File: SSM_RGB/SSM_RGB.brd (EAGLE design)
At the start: 80.1 x 68.8 mm, 12 parts

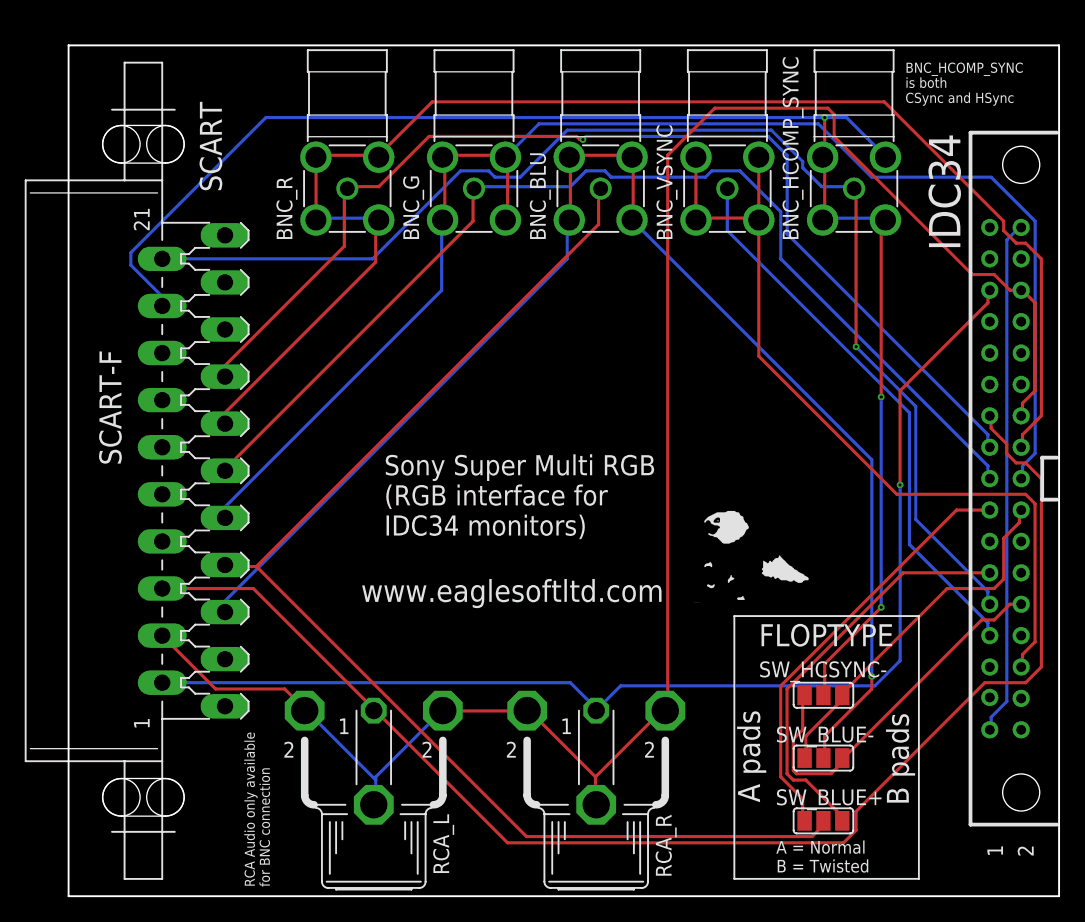
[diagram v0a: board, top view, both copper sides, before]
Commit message: Final PCB revisions
SSM & X:
*Renamed BNC_HComp_Sync to just BNC_HCSYNC
*Renamed "Normal" cable type to "Nonstd"
*Removed stray line segs in PCB Art

SSM:
*Added warning about using both AV sources

X:
*Renamed VReg and Bus Sw IC components to Ux series
*Renamed both switchs to Sx series
*Renamed "PWR" to "J1"

Documentation:
*1st draft. Needs final product photos/images, and list of component names+parts
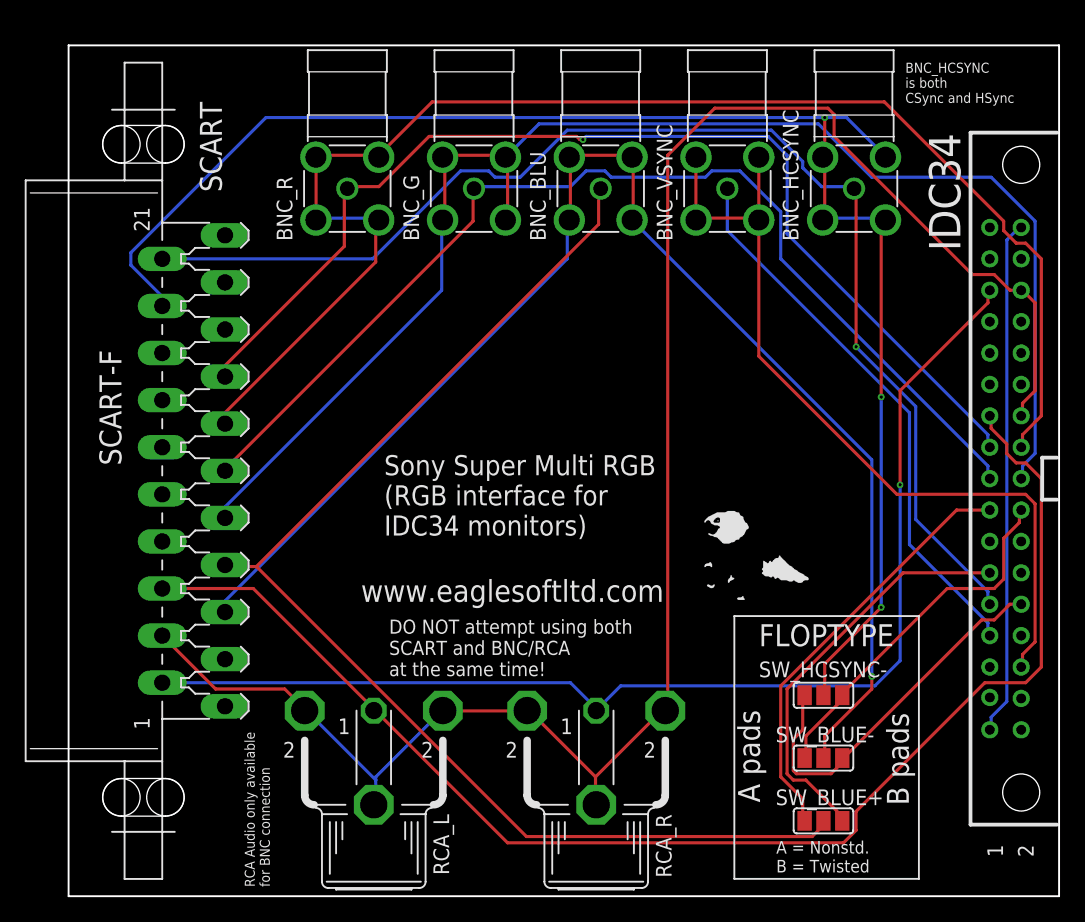
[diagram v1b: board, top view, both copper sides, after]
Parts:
- renumbered BNC_HCOMP_SYNC to BNC_HCSYNC
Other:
- board text added: "A = Nonstd. B = Twisted"
- board text added: "BNC_HCSYNC is both CSync and HSync"
- board text added: "DO NOT attempt using both SCART and BNC/RCA at the same time!"
- board text removed: "A = Normal B = Twisted"
- board text removed: "BNC_HCOMP_SYNC is both CSync and HSync"
- board text removed: "C:/Users/Anthony/Documents/eagle/SSM/Artwork/Large/p1m.bmp"
- board text removed: "C:/Users/Anthony/Documents/eagle/SSM/Artwork/Large/p2m.bmp"
- board text removed: "C:/Users/Anthony/Documents/eagle/SSM/Artwork/Large/p3m.bmp"
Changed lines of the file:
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@@
 (RGB interface for
 IDC34 monitors)</text>
-<text x="137.2997" y="36.72205" size="1.016" layer="21">A = Normal
+<text x="137.2997" y="36.72205" size="1.016" layer="21">A = Nonstd.
 B = Twisted</text>
-<text x="147.74545" y="98.97745" size="0.8128" layer="21">BNC_HCOMP_SYNC
+<text x="147.74545" y="98.97745" size="0.8128" layer="21">BNC_HCSYNC
 is both
 CSync and HSync</text>
@@
 <rectangle x1="135.912225" y1="71.034275" x2="136.998075" y2="71.040625" layer="17"/>
 <rectangle x1="135.912225" y1="71.040625" x2="136.998075" y2="71.046975" layer="17"/>
-<text x="130.63855" y="58.52795" size="0.0127" layer="17" font="vector">C:/Users/Anthony/Documents/eagle/SSM/Artwork/Large/p1m.bmp</text>
 <rectangle x1="134.750175" y1="58.874025" x2="134.877175" y2="58.880375" layer="29"/>
 <rectangle x1="134.750175" y1="58.880375" x2="134.877175" y2="58.886725" layer="29"/>
@@
 <rectangle x1="135.912225" y1="71.034275" x2="136.998075" y2="71.040625" layer="29"/>
 <rectangle x1="135.912225" y1="71.040625" x2="136.998075" y2="71.046975" layer="29"/>
-<text x="130.63855" y="58.52795" size="0.0127" layer="29" font="vector">C:/Users/Anthony/Documents/eagle/SSM/Artwork/Large/p1m.bmp</text>
 <rectangle x1="139.087225" y1="60.144025" x2="139.322175" y2="60.150375" layer="21"/>
 <rectangle x1="139.087225" y1="60.150375" x2="139.322175" y2="60.156725" layer="21"/>
@@
 <rectangle x1="133.372225" y1="65.954275" x2="133.924675" y2="65.960625" layer="21"/>
 <rectangle x1="133.372225" y1="65.960625" x2="133.924675" y2="65.966975" layer="21"/>
-<text x="130.63855" y="58.52795" size="0.0127" layer="21" font="vector">C:/Users/Anthony/Documents/eagle/SSM/Artwork/Large/p2m.bmp</text>
 <rectangle x1="134.223125" y1="58.766075" x2="134.724775" y2="58.772425" layer="25"/>
 <rectangle x1="134.223125" y1="58.772425" x2="134.724775" y2="58.778775" layer="25"/>
@@
 <rectangle x1="131.949825" y1="61.820425" x2="131.975225" y2="61.826775" layer="25"/>
 <rectangle x1="131.949825" y1="61.826775" x2="131.975225" y2="61.833125" layer="25"/>
-<text x="130.63855" y="58.52795" size="0.0127" layer="25" font="vector">C:/Users/Anthony/Documents/eagle/SSM/Artwork/Large/p3m.bmp</text>
+<text x="105.9815" y="52.6034" size="1.143" layer="25">DO NOT attempt using both
+SCART and BNC/RCA
+at the same time!</text>
 </plain>
 <attributes>
@@
 <elements>
 <element name="IDC34" library="con-3m-skt-header" package="S34RA" value="" x="160.02" y="68.58" rot="R270"/>
-<element name="BNC_HCOMP_SYNC" library="amphenol-142142_10" package="142142" value="142142" x="143.5989" y="92.04325" smashed="yes" rot="R90">
+<element name="BNC_HCSYNC" library="amphenol-142142_10" package="142142" value="142142" x="143.5989" y="92.04325" smashed="yes" rot="R90">
 <attribute name="MF" value="Amphenol Connex" x="143.5989" y="92.04325" size="1.778" layer="27" rot="R90" display="off"/>
 <attribute name="MPN" value="" x="143.5989" y="92.04325" size="1.778" layer="27" rot="R90" display="off"/>
@@
 <attribute name="OC_FARNELL" value="592791" x="122.73915" y="47.27575" size="1.778" layer="27" rot="R180" display="off"/>
 <attribute name="OC_NEWARK" value="06WX5914" x="122.73915" y="47.27575" size="1.778" layer="27" rot="R180" display="off"/>
-<attribute name="VALUE" x="116.64315" y="41.43375" size="1.27" layer="27" ratio="10" rot="R270"/>
 </element>
 <element name="SCART" library="con-hirschmann" library_urn="urn:adsk.eagle:library:153" package="SCART-F" package3d_urn="urn:adsk.eagle:package:7461/1" value="SCART-F" x="87.63" y="69.215" rot="R270">
@@
 <contactref element="IDC34" pad="9"/>
 <contactref element="SCART" pad="20"/>
-<contactref element="BNC_HCOMP_SYNC" pad="1"/>
+<contactref element="BNC_HCSYNC" pad="1"/>
 <wire x1="154.432" y1="59.436" x2="154.432" y2="58.42" width="0.254" layer="16"/>
 <wire x1="148.59" y1="65.278" x2="154.432" y2="59.436" width="0.254" layer="16"/>
@@
 <signal name="HCOMP_SYNC-">
 <contactref element="SCART" pad="18"/>
-<contactref element="BNC_HCOMP_SYNC" pad="3"/>
-<contactref element="BNC_HCOMP_SYNC" pad="2"/>
-<contactref element="BNC_HCOMP_SYNC" pad="4"/>
-<contactref element="BNC_HCOMP_SYNC" pad="5"/>
+<contactref element="BNC_HCSYNC" pad="3"/>
+<contactref element="BNC_HCSYNC" pad="2"/>
+<contactref element="BNC_HCSYNC" pad="4"/>
+<contactref element="BNC_HCSYNC" pad="5"/>
 <contactref element="SW_HCSYNC-" pad="2"/>
 <wire x1="141.224" y1="94.488" x2="141.224" y2="89.662" width="0.254" layer="1"/>
